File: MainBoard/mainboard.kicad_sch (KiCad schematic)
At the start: 3 parts, among them J1 MatrixOut, J4 MatrixPin, J5 PowerIn

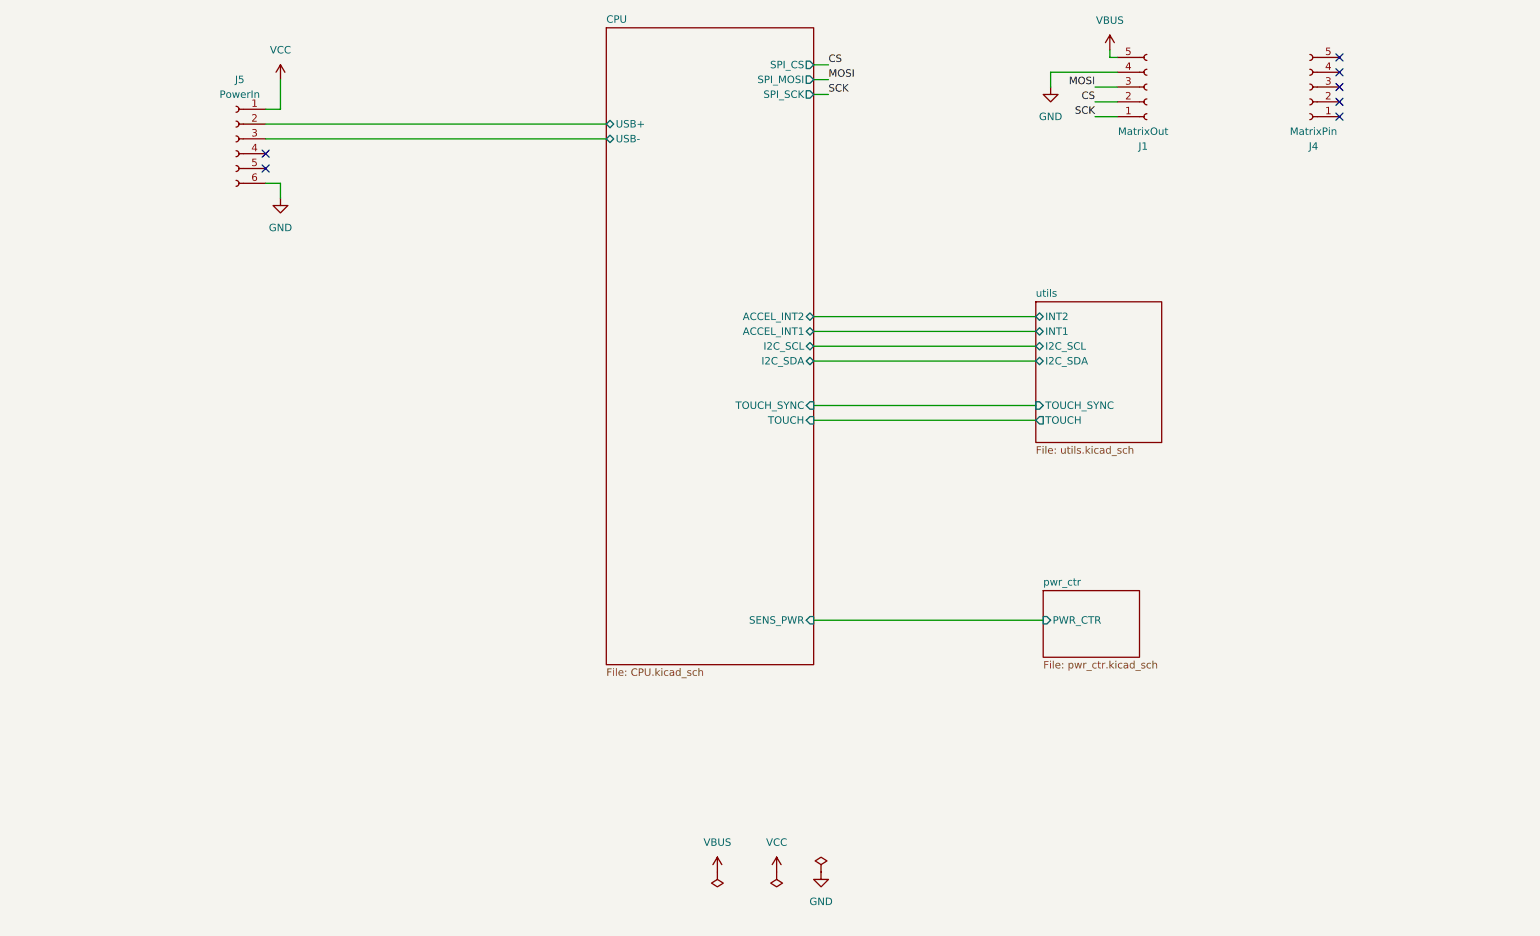
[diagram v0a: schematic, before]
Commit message: change schematic, use touch controller to enable second bard power. microcontroller should set pin up to latch power
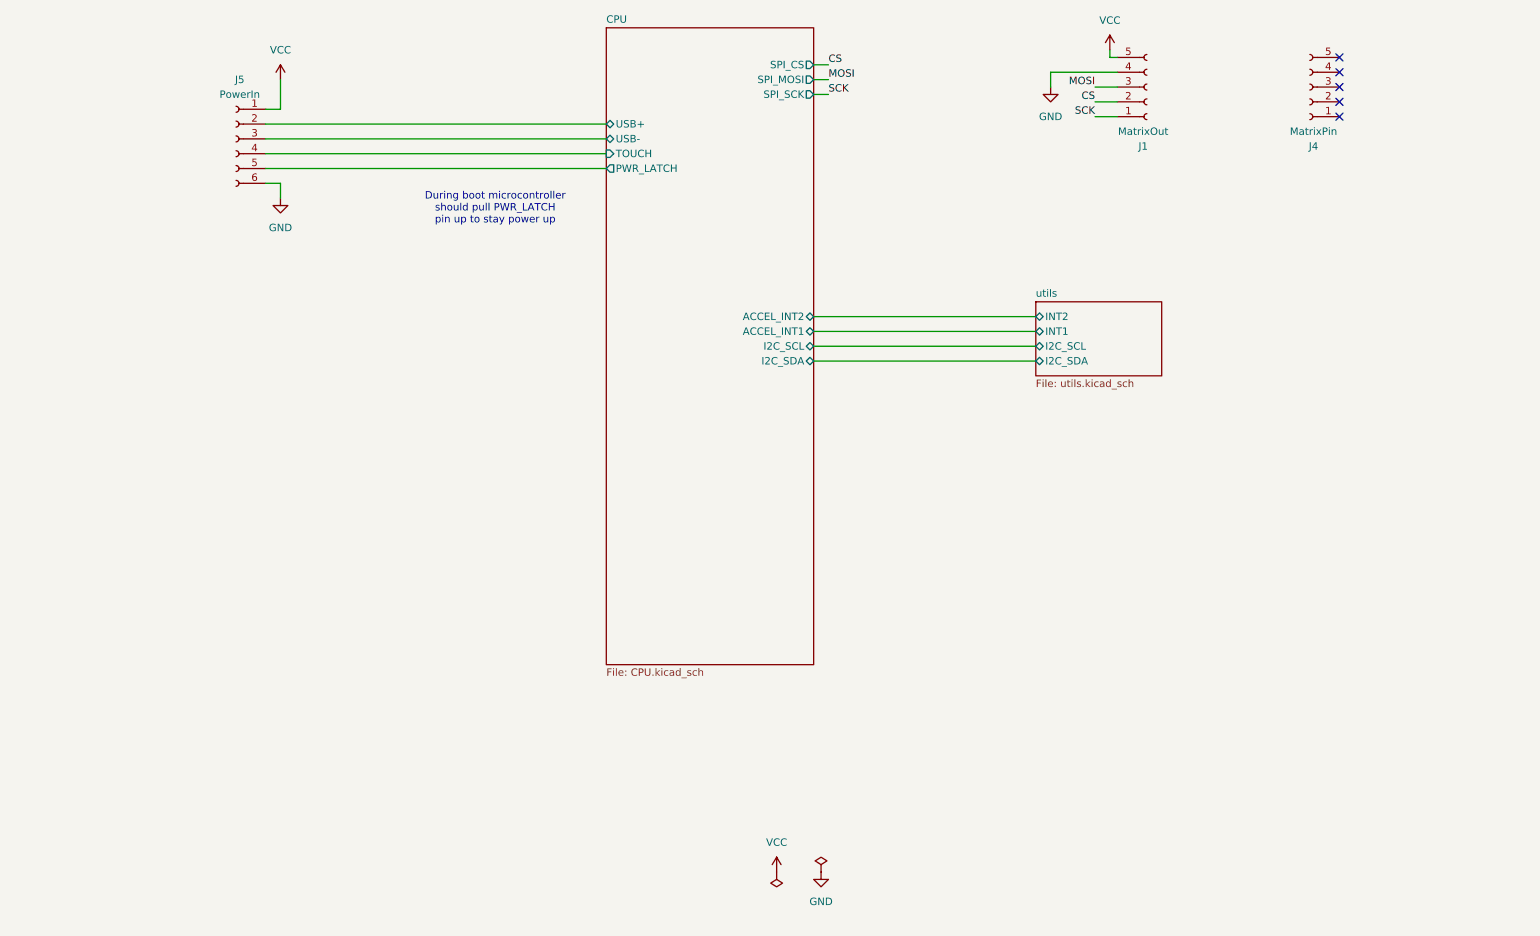
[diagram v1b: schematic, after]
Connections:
- net VBUS is gone; now on net VCC: J1.5 (Pin_5)
- net CPU/TOUCH: now also J5.4 (Pin_4)
- net CPU/PWR_LATCH: now reaches J5.5 (Pin_5)
- no-connect marks 7 -> 5
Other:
- removed sheet pwr_ctr
- sheet CPU ports: added PWR_LATCH; removed SENS_PWR, TOUCH_SYNC
- sheet utils ports: added none; removed TOUCH, TOUCH_SYNC
- note added: "During boot microcontroller should pull PWR_LATCH pin up to stay power up"

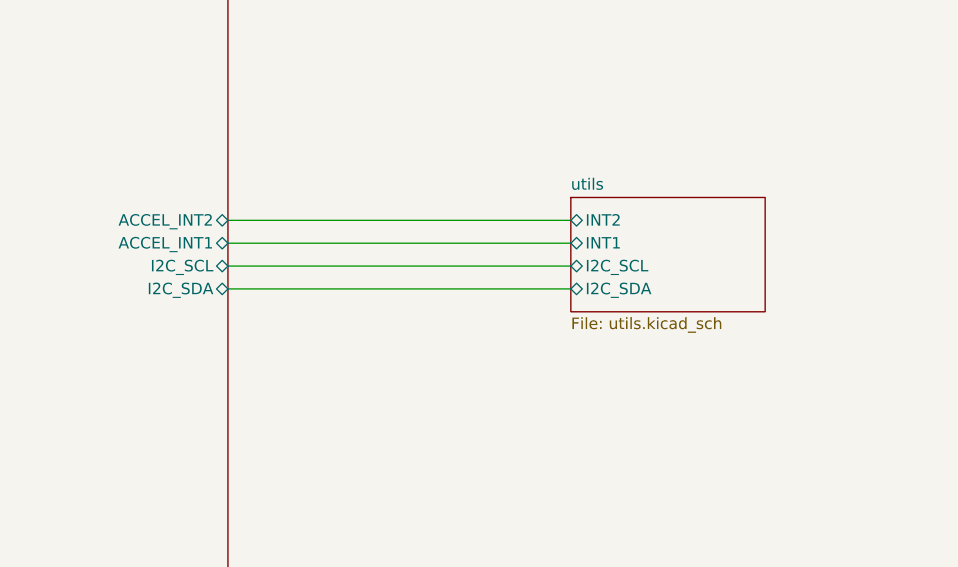
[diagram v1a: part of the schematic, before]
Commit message: Change location of tuch sensor, touch button now power up all components, change length. Add buzzer to mainboard and remove touch from them. change revision version
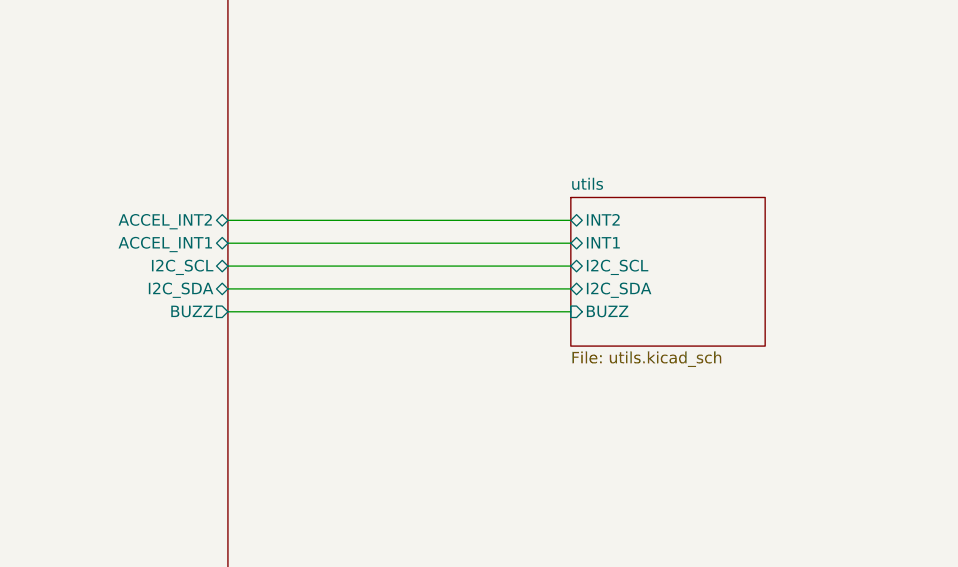
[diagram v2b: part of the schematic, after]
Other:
- sheet CPU ports: added BUZZ; removed none
- sheet utils ports: added BUZZ; removed none
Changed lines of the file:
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@@
 		(title "blob")
 		(date "2025-09-15")
-		(rev "3")
+		(rev "0.4.0")
 		(company "Miłosz Derżko")
 	)
@@
 		(pts
 			(xy 64.77 58.42) (xy 123.19 58.42)
+		)
+		(stroke
+			(width 0)
+			(type default)
+		)
+	)
+	(wire
+		(pts
+			(xy 158.75 93.98) (xy 196.85 93.98)
 		)
 		(stroke
@@
 	(sheet
 		(at 196.85 81.28)
-		(size 21.59 12.7)
+		(size 21.59 16.51)
 		(exclude_from_sim no)
 		(in_bom yes)
@@
 		)
 		(property "Sheetfile" "utils.kicad_sch"
-			(at 196.85 94.5646 0)
+			(at 196.85 98.3746 0)
 			(effects
 				(font
@@
 		(pin "INT2" bidirectional
 			(at 196.85 83.82 180)
+			(effects
+				(font
+					(size 1.27 1.27)
+				)
+				(justify left)
+			)
+		)
+		(pin "BUZZ" input
+			(at 196.85 93.98 180)
 			(effects
 				(font
@@
 			)
 		)
+		(pin "BUZZ" output
+			(at 158.75 93.98 0)
+			(effects
+				(font
+					(size 1.27 1.27)
+				)
+				(justify right)
+			)
+		)

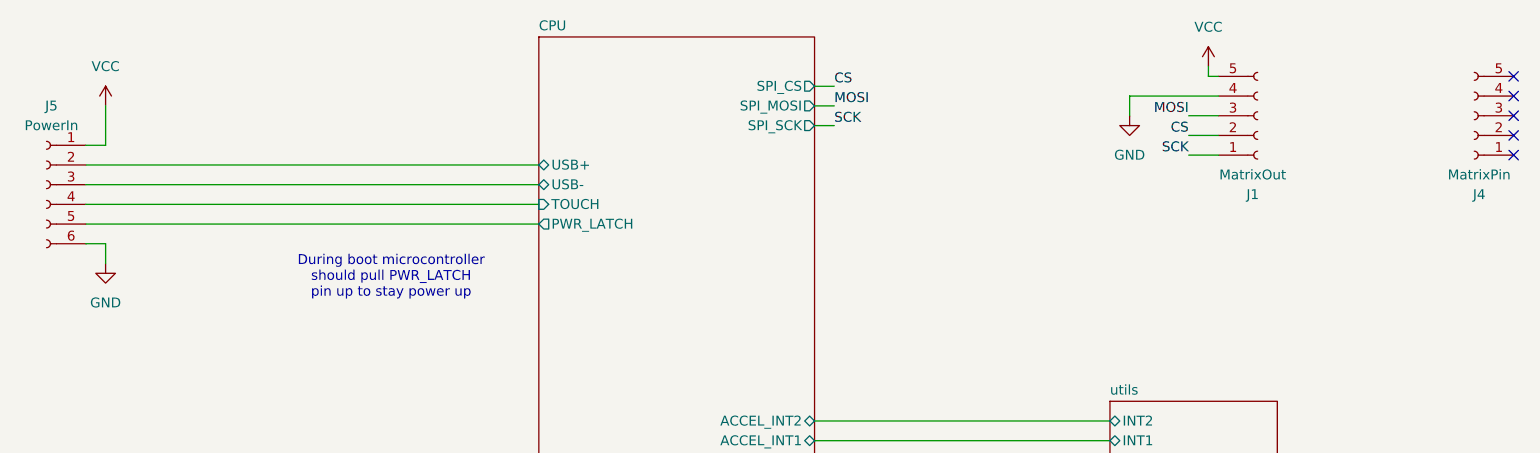
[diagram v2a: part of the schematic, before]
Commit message: some changes for esp32 board
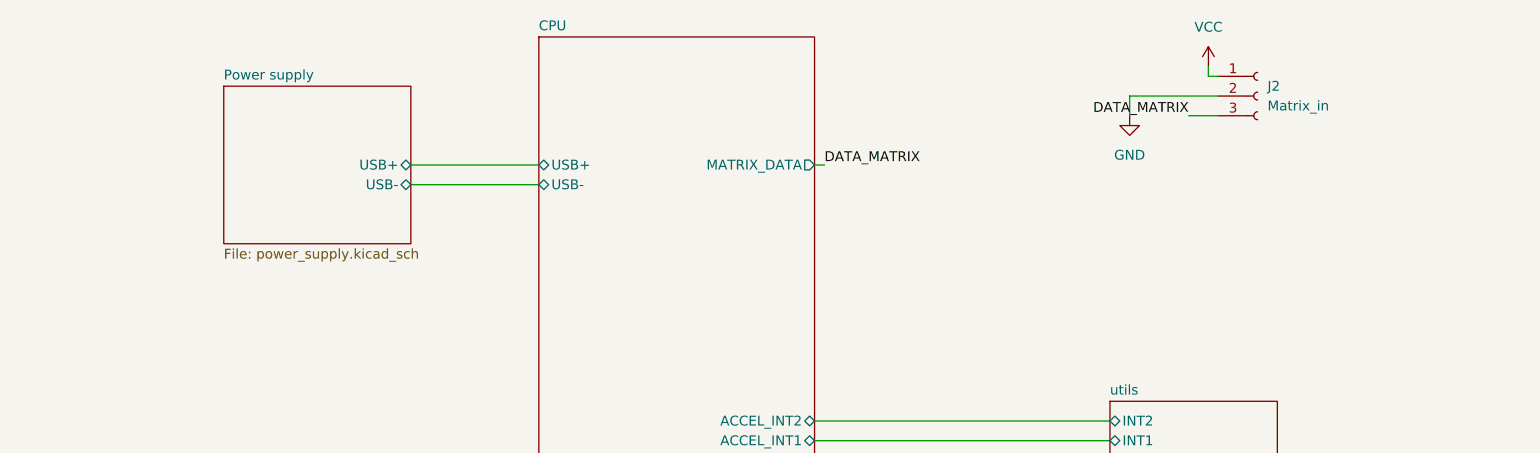
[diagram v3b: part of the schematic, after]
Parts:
- removed J1: MatrixOut, Connector_PinSocket_2.54mm:PinSocket_1x05_P2.54mm_Vertical, symbol Connector:Conn_01x05_Socket
- removed J4: MatrixPin, Connector_PinSocket_2.54mm:PinSocket_1x05_P2.54mm_Vertical, symbol Connector:Conn_01x05_Socket
- removed J5: PowerIn, EdgeConn:edge_conn_03x02_1_6x10mm_socket, symbol Connector:Conn_01x06_Socket
- added J2: Matrix_in, Connector_PinSocket_2.54mm:PinSocket_1x03_P2.54mm_Vertical, symbol Connector:Conn_01x03_Socket
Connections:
- net GND: now also J2.2 (Pin_2)
- net VCC: now also J2.1 (Pin_1)
- new net DATA_MATRIX: J2.3 (Pin_3)
- no-connect marks 5 -> 0
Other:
- added sheet Power supply (power_supply.kicad_sch)
- sheet CPU ports: added MATRIX_DATA; removed PWR_LATCH, SPI_CS, SPI_MOSI, SPI_SCK, TOUCH
- note removed: "During boot microcontroller should pull PWR_LATCH pin up to stay power up"

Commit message: change schematic
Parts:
- removed J2: Matrix_in, Connector_PinSocket_2.54mm:PinSocket_1x03_P2.54mm_Vertical, symbol Connector:Conn_01x03_Socket
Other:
- sheet CPU ports: added TOUCH; removed none
- sheet utils ports: added DATA_MATRIX, TOUCH; removed none

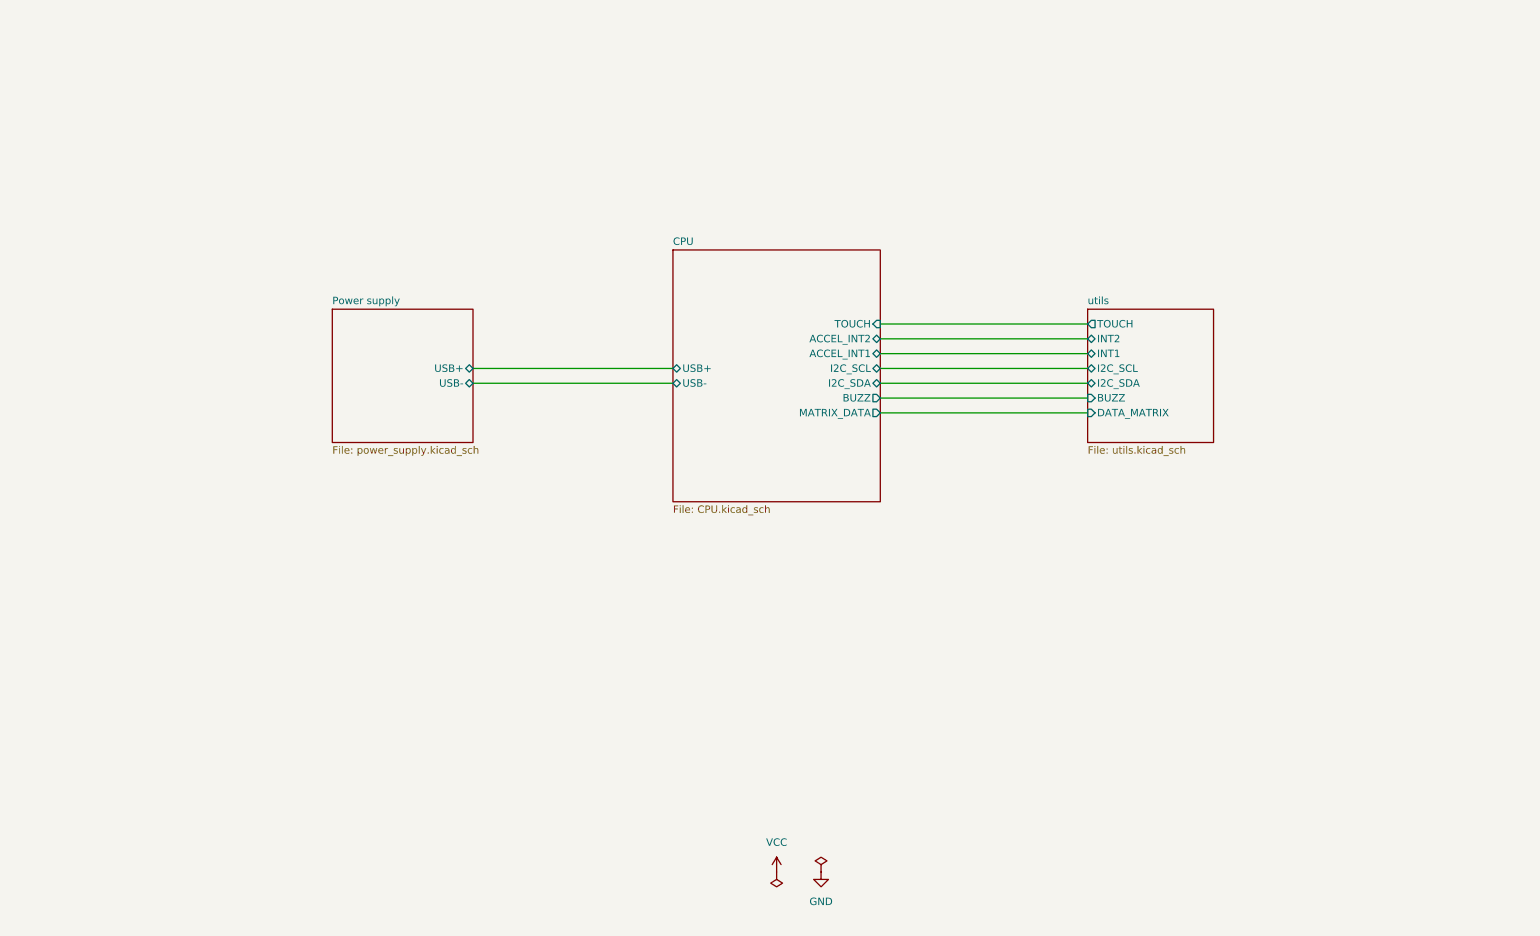
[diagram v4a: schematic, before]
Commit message: Change project assumptions, create new board with esp32-c3
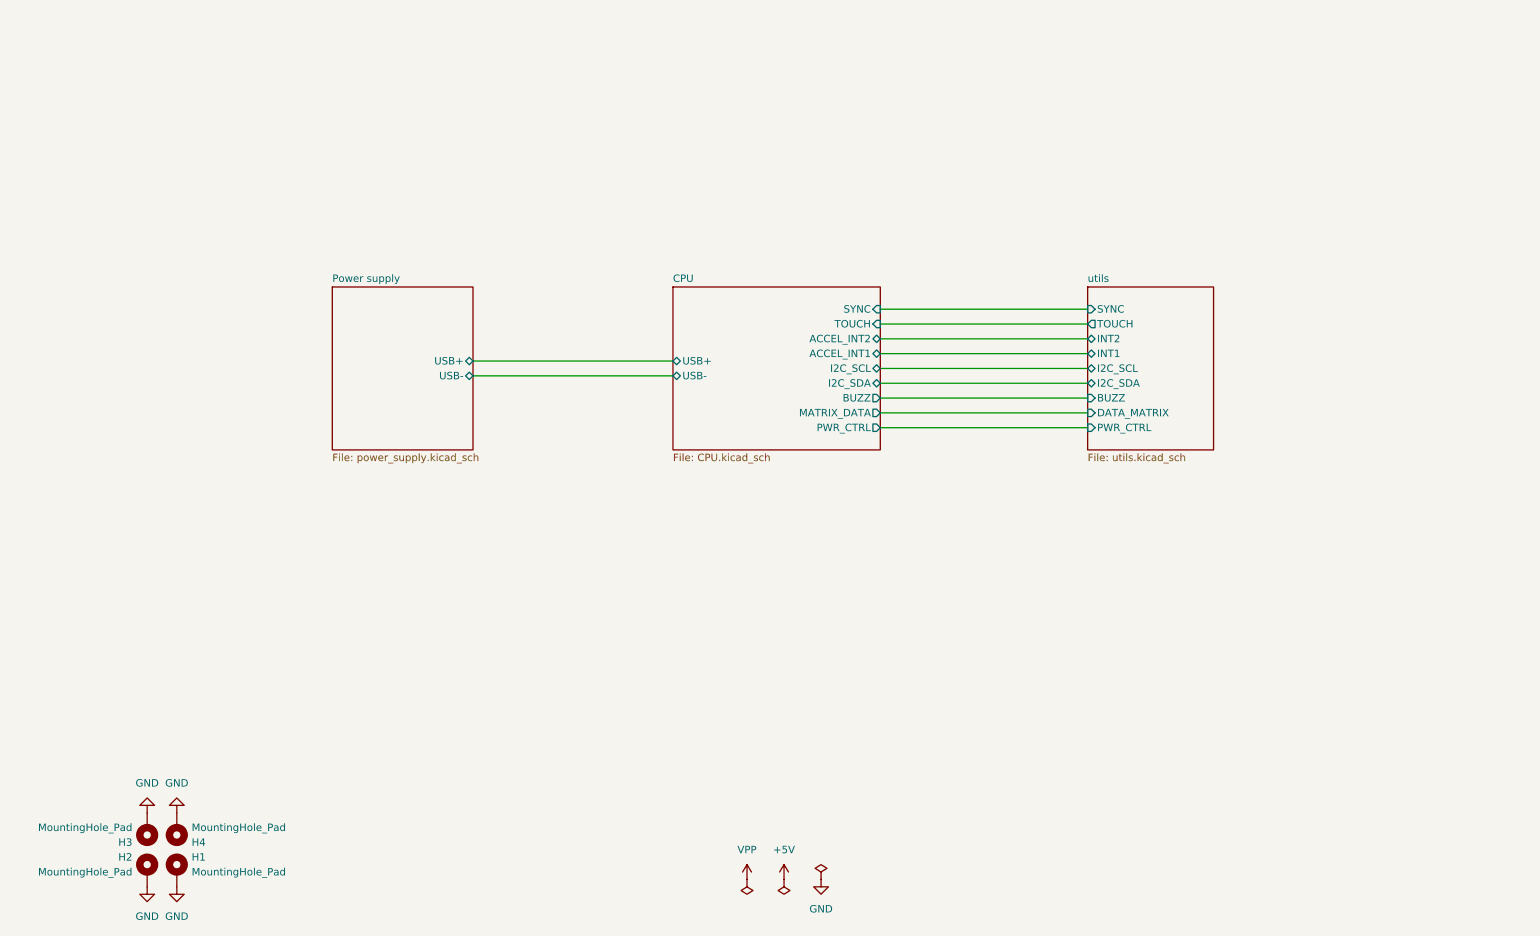
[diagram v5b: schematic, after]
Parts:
- added H1, H2, H3, H4: MountingHole_Pad, MountingHole:MountingHole_2.5mm, symbol Mechanical:MountingHole_Pad
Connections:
- net GND: now also H1.1, H2.1, H3.1, H4.1
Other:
- sheet CPU ports: added PWR_CTRL, SYNC; removed none
- sheet utils ports: added PWR_CTRL, SYNC; removed none

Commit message: Udpate project variables and add texts
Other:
- title: blob -> VirtualBlob
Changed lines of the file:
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@@
 	(paper "A4")
 	(title_block
-		(title "blob")
+		(title "VirtualBlob")
 		(date "2025-09-15")
 		(rev "0.4.0")

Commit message: Change naming of project
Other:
- company: Miłosz Derżko -> ${Company}
- title: VirtualBlob -> ${ProjectTitle}
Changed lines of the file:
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@@
 	(paper "A4")
 	(title_block
-		(title "VirtualBlob")
+		(title "${ProjectTitle}")
 		(date "2025-09-15")
-		(rev "0.4.0")
-		(company "Miłosz Derżko")
+		(rev "${Revision}")
+		(company "${Company}")
 	)
 	(wire
@@
 		)
 		(instances
-			(project "mainboard"
+			(project "MainBoard"
 				(path "/9e709b97-b403-4027-b7d8-a3ed3b3557e2"
 					(reference "#PWR056")
@@
 		)
 		(instances
-			(project "mainboard"
+			(project "MainBoard"
 				(path "/9e709b97-b403-4027-b7d8-a3ed3b3557e2"
 					(reference "H2")
@@
 		)
 		(instances
-			(project "mainboard"
+			(project "MainBoard"
 				(path "/9e709b97-b403-4027-b7d8-a3ed3b3557e2"
 					(reference "#FLG03")
@@
 		)
 		(instances
-			(project "mainboard"
+			(project "MainBoard"
 				(path "/9e709b97-b403-4027-b7d8-a3ed3b3557e2"
 					(reference "H3")
@@
 		)
 		(instances
-			(project "mainboard"
+			(project "MainBoard"
 				(path "/9e709b97-b403-4027-b7d8-a3ed3b3557e2"
 					(reference "#PWR055")
@@
 		)
 		(instances
-			(project "mainboard"
+			(project "MainBoard"
 				(path "/9e709b97-b403-4027-b7d8-a3ed3b3557e2"
 					(reference "#PWR023")
@@
 		)
 		(instances
-			(project "mainboard"
+			(project "MainBoard"
 				(path "/9e709b97-b403-4027-b7d8-a3ed3b3557e2"
 					(reference "#FLG01")
@@
 		)
 		(instances
-			(project "mainboard"
+			(project "MainBoard"
 				(path "/9e709b97-b403-4027-b7d8-a3ed3b3557e2"
 					(reference "#PWR058")
@@
 		)
 		(instances
-			(project "mainboard"
+			(project "MainBoard"
 				(path "/9e709b97-b403-4027-b7d8-a3ed3b3557e2"
 					(reference "H4")
@@
 		)
 		(instances
-			(project "mainboard"
+			(project "MainBoard"
 				(path "/9e709b97-b403-4027-b7d8-a3ed3b3557e2"
 					(reference "#FLG04")
@@
 		)
 		(instances
-			(project "mainboard"
+			(project "MainBoard"
 				(path "/9e709b97-b403-4027-b7d8-a3ed3b3557e2"
 					(reference "#PWR057")
@@
 		)
 		(instances
-			(project "mainboard"
+			(project "MainBoard"
 				(path "/9e709b97-b403-4027-b7d8-a3ed3b3557e2"
 					(reference "#PWR07")
@@
 		)
 		(instances
-			(project "mainboard"
+			(project "MainBoard"
 				(path "/9e709b97-b403-4027-b7d8-a3ed3b3557e2"
 					(reference "#PWR013")
